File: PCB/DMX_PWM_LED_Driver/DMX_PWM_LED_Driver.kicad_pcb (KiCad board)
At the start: 2 copper layers, 100 x 45 mm, 51 parts, among them J1 Programming_Header, J2 PWR_OUT, J3 PWR_IN, J4 LED_OUT, J5 Conn_Left, J6 Conn_Right, Q1 IRLZ44N, SW1 SW_SPST, SW2 SW_DIP_x04, U2 MAX485E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

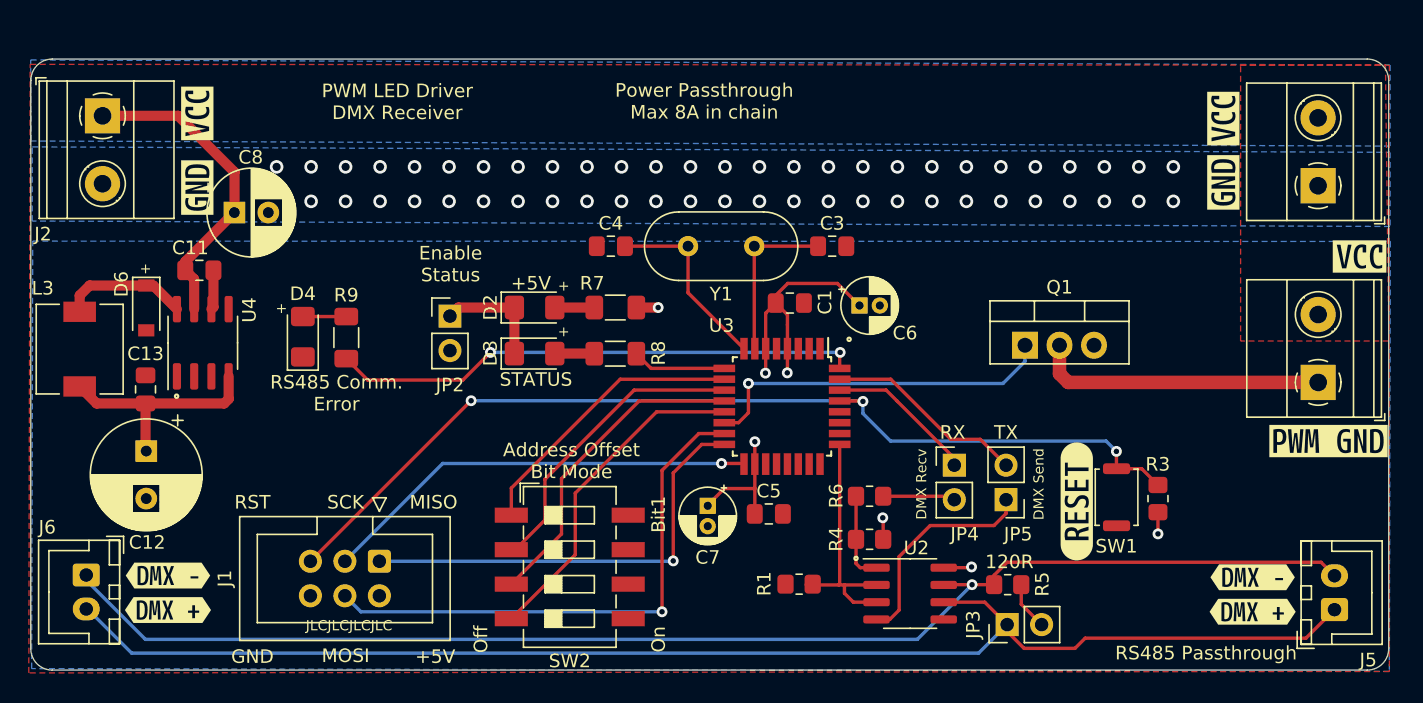
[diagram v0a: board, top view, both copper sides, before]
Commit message: Updated design of PWM board and code updated for slave boards
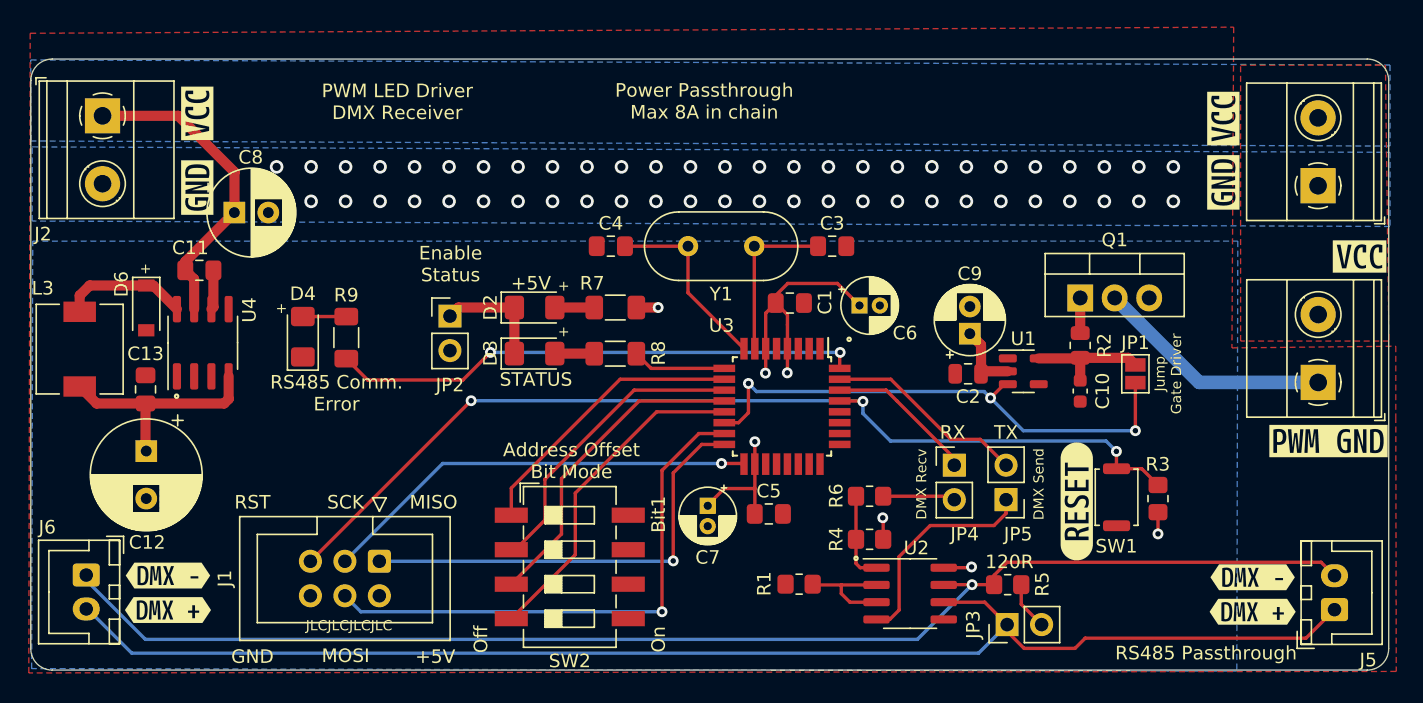
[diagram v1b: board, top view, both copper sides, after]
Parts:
- added C10: 1nF, Capacitor_SMD:C_0603_1608Metric, F.Cu at (97.3, 44.5)
- added C2: 100nF, Capacitor_SMD:C_0805_2012Metric, F.Cu at (89.0, 43.2)
- added C9: 1uF, Capacitor_THT:CP_Radial_D5.0mm_P2.00mm, F.Cu at (89.2, 40.2)
- added JP1: Jump_Gate_Driver, Jumper:SolderJumper-2_P1.3mm_Open_Pad1.0x1.5mm, F.Cu at (101.3, 43.2)
- added R2: 10R, Resistor_SMD:R_0805_2012Metric, F.Cu at (97.3, 41.1)
- added U1: MCP1416, Package_TO_SOT_SMD:SOT-23-5, F.Cu at (93.1, 43.0)
- moved Q1 5.35 mm to (97.3, 37.6)
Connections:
- Q1 pad 1: LED_PWM -> Net-(Q1-Pad1)
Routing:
- net LED_PWM: track 26.5 -> 39.4 mm, vias 1 -> 3
- net Net-(R1-Pad1): track 18.8 -> 8.22 mm
- net Net-(C10-Pad1): track 0.00 -> 9.02 mm
- net +5V: track 51.8 -> 57.1 mm
- net Net-(J4-Pad1): track 21.4 -> 17.6 mm
- net Net-(Q1-Pad1): track 0.00 -> 2.59 mm
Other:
- board text added: "Jump Gate Driver"
